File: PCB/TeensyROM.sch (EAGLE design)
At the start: 2 parts, among them P1 MA22-2, U1 TEENSY41-STRIP

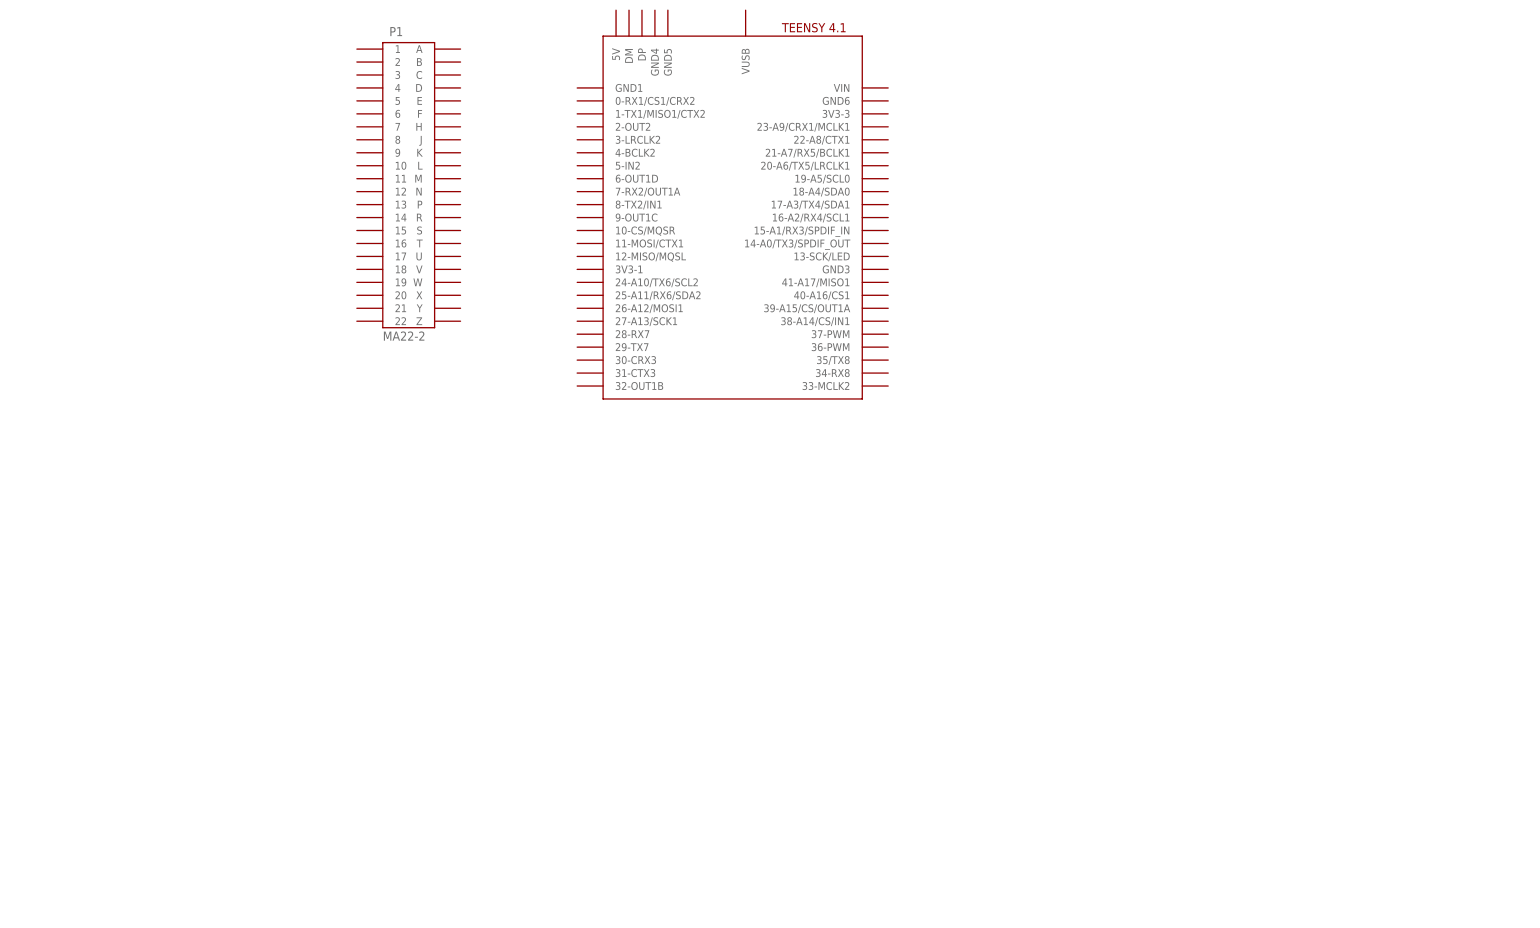
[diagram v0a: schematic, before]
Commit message: DMA/NMI pins
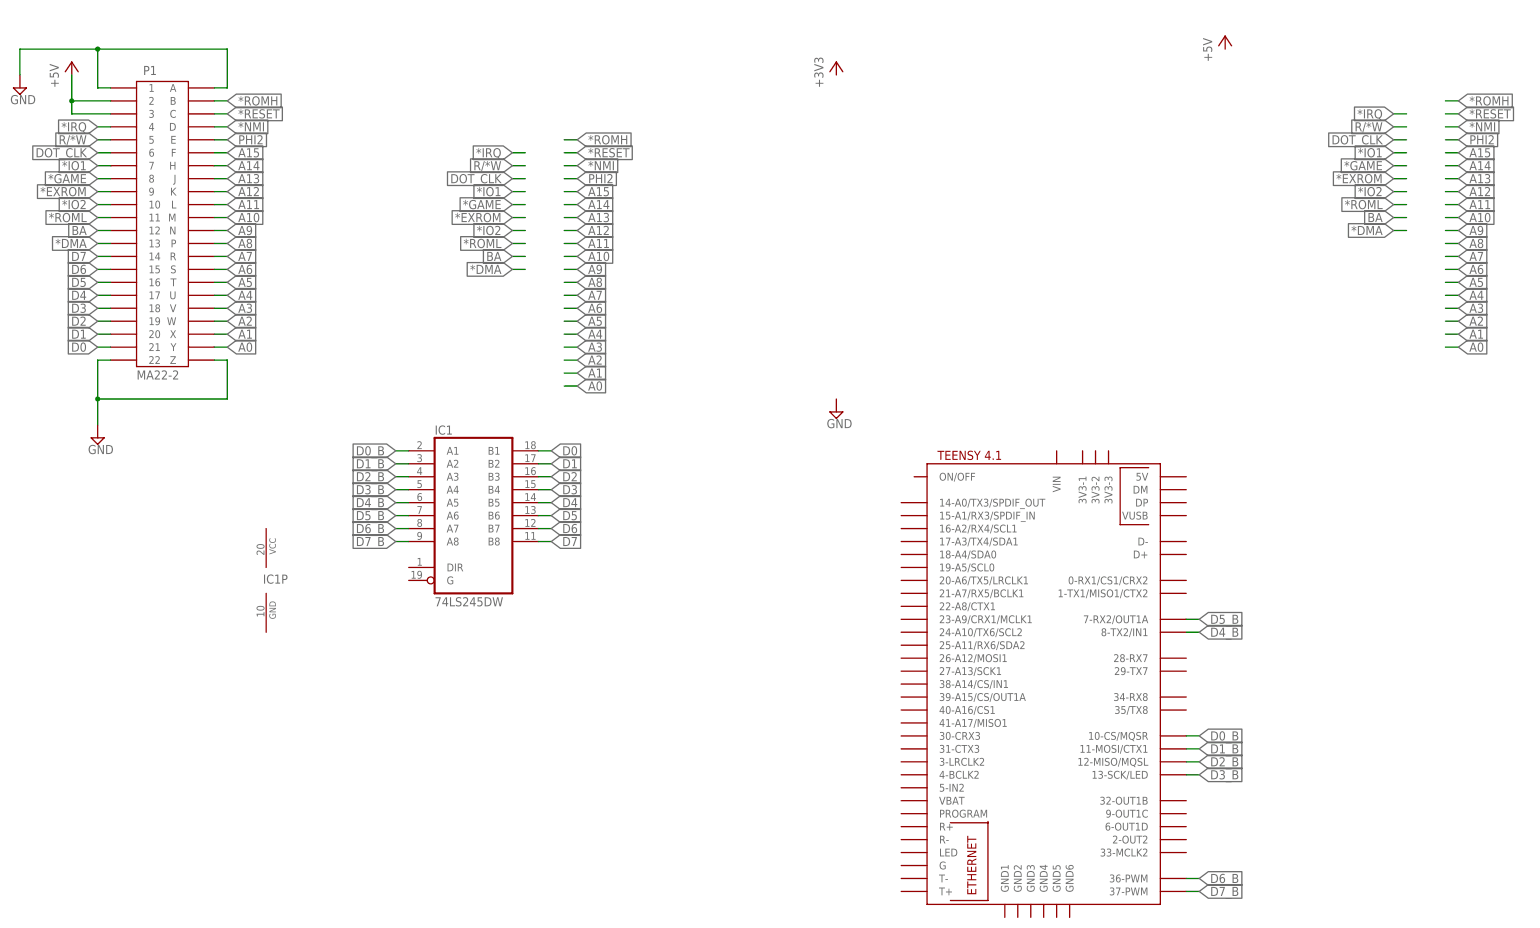
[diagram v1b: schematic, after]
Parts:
- removed U1: TEENSY41-STRIP, teensy:TEENSY41-STRIP
- added IC1: 74LS245DW, 74xx-us:74LS245DW
- added U$1: TEENSY41, teensy:TEENSY41
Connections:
- new net *DMA: P1.13
- new net *EXROM: P1.9
- new net *GAME: P1.8
- new net *IO1: P1.7
- new net *IO2: P1.10
- new net *IRQ: P1.4
- new net *NMI: P1.D
- new net *RESET: P1.C
- new net *ROMH: P1.B
- new net *ROML: P1.11
- new net +5V: P1.2, P1.3
- new net A0: P1.Y
- new net A1: P1.X
- new net A10: P1.M
- new net A11: P1.L
- new net A12: P1.K
- new net A13: P1.J
- new net A14: P1.H
- new net A15: P1.F
- new net A2: P1.W
- new net A3: P1.V
- new net A4: P1.U
- new net A5: P1.T
- new net A6: P1.S
- new net A7: P1.R
- new net A8: P1.P
- new net A9: P1.N
- new net BA: P1.12
- new net D0: IC1A.B1, P1.21
- new net D0_B: IC1A.A1, U$1.10-CS/MQSR
- new net D1: IC1A.B2, P1.20
- new net D1_B: IC1A.A2, U$1.11-MOSI/CTX1
- new net D2: IC1A.B3, P1.19
- new net D2_B: IC1A.A3, U$1.12-MISO/MQSL
- new net D3: IC1A.B4, P1.18
- new net D3_B: IC1A.A4, U$1.13-SCK/LED
- new net D4: IC1A.B5, P1.17
- new net D4_B: IC1A.A5, U$1.8-TX2/IN1
- new net D5: IC1A.B6, P1.16
- new net D5_B: IC1A.A6, U$1.7-RX2/OUT1A
- new net D6: IC1A.B7, P1.15
- new net D6_B: IC1A.A7, U$1.36-PWM
- new net D7: IC1A.B8, P1.14
- new net D7_B: IC1A.A8, U$1.37-PWM
- new net DOT_CLK: P1.6
- new net GND: P1.1, P1.22, P1.A, P1.Z
- new net PHI2: P1.E
- new net R/*W: P1.5
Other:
- moved on the sheet: P1

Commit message: schem updates
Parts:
- removed P1: MA22-2, con-edge-100:44PINEDGE
- added B9: SW-MOM, AudioLooper:SWITCH-MOMENTARY-2PTH
- added C1, C3: (no value), rcl:CPOL-USE2.5-6
- added C2: (no value), rcl:CPOL-EUA/3216-18W
- added D5: RED, Dolphin v3.20:LED-3MM-RED
- added D6: GRN, Dolphin v3.20:LED-3MM-GRN
- added IC2, IC3, IC4: 74LS245DW, 74xx-us:74LS245DW
- added IC5: 74LS07D, 74xx-us:74LS07D
- added J1: C64-EXPANSION-PORT, Commodore:C64-EXPANSIONPNARROW
- added J2: (no value), AudioLooper:USB-787616
- added JP1: (no value), pinhead:PINHD-2X22
- added R6: 4.7k, resistor:R-US_R0805
- added X1: SI-50170, con-stewart:SI-50170
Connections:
- removed net *DMA: P1.13
- removed net *EXROM: P1.9
- removed net *GAME: P1.8
- removed net *IO1: P1.7
- removed net *IO2: P1.10
- removed net *IRQ: P1.4
- removed net *NMI: P1.D
- removed net *RESET: P1.C
- removed net *ROMH: P1.B
- removed net *ROML: P1.11
- removed net R/*W: P1.5
- new net !DMA: J1.!DMA
- new net !EXROM: J1.!EXROM
- new net !GAME: J1.!GAME
- new net !IO1: J1.!I/O1
- new net !IO2: J1.!I/O2
- new net !IRQ: J1.!IRQ
- new net !NMI: J1.!NMI
- new net !RESET: J1.!RESET
- new net !ROMH: J1.!ROMH
- new net !ROML: J1.!ROML
- new net +3V3: IC1P.VCC, U$1.3V3-1, U$1.3V3-2, U$1.3V3-3
- new net +5V1: C1.+
- new net B12: D5.C
- new net D+: J2.3
- new net D-: J2.2
- new net GND1: J1.GND@A, J1.GND@Z
- new net GND2: D6.C
- new net GND3: C1.-
- new net N$1: D6.A, R6.1
- new net N$5: D5.A
- new net R/!W: J1.R/!W
- new net USB5V: C2.+, J2.1
- new net VCC1: R6.2
- net +5V: now also J1.+5V@2, J1.+5V@3; no longer P1.2, P1.3
- net A0: now also IC2A.B1, J1.A0; no longer P1.Y
- net A1: now also IC2A.B2, J1.A1; no longer P1.X
- net A10: now also J1.A10; no longer P1.M
- net A11: now also J1.A11; no longer P1.L
- net A12: now also J1.A12; no longer P1.K
- net A13: now also J1.A13; no longer P1.J
- net A14: now also J1.A14; no longer P1.H
- net A15: now also J1.A15; no longer P1.F
- net A2: now also IC2A.B3, J1.A2; no longer P1.W
- net A3: now also IC2A.B4, J1.A3; no longer P1.V
- net A4: now also IC2A.B5, J1.A4; no longer P1.U
- net A5: now also IC2A.B6, J1.A5; no longer P1.T
- net A6: now also IC2A.B7, J1.A6; no longer P1.S
- net A7: now also IC2A.B8, J1.A7; no longer P1.R
- net A8: now also J1.A8; no longer P1.P
- net A9: now also J1.A9; no longer P1.N
- net BA: now also J1.BA; no longer P1.12
- net D0: now also J1.D0; no longer P1.21
- net D1: now also J1.D1; no longer P1.20
- net D2: now also J1.D2; no longer P1.19
- net D3: now also J1.D3; no longer P1.18
- net D4: now also J1.D4; no longer P1.17
- net D5: now also J1.D5; no longer P1.16
- net D6: now also J1.D6; no longer P1.15
- net D7: now also J1.D7; no longer P1.14
- net DOT_CLK: now also J1.DOT_CLOCK; no longer P1.6
- net GND: now also C2.-, IC1P.GND, J1.GND@1, J1.GND@22, J2.4, J2.5, J2.6, U$1.GND1, U$1.GND2, U$1.GND3, U$1.GND4, U$1.GND5, U$1.GND6; no longer P1.1, P1.22, P1.A, P1.Z
- net PHI2: now also J1.PHI2; no longer P1.E
